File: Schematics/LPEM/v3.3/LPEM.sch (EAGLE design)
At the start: 40 parts, among them IC1 7805, IC2 PCA9600SO8, IC3 7803, IC4 7810, Q1 12MHz, U1 STM32F303K8T6, U2 MAX3421E

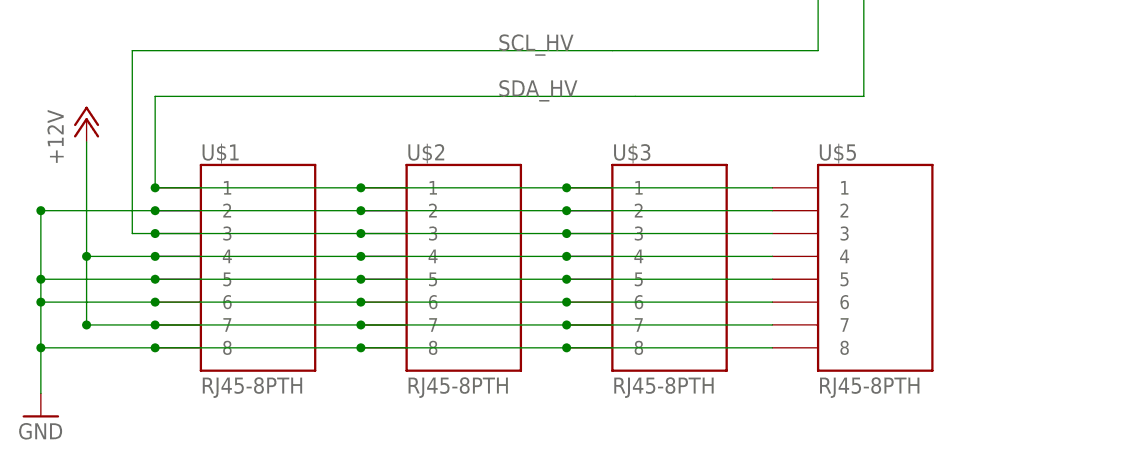
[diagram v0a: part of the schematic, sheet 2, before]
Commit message: Add LPEM v3.3, which will probably never be produced, and a few cleanups to other files.
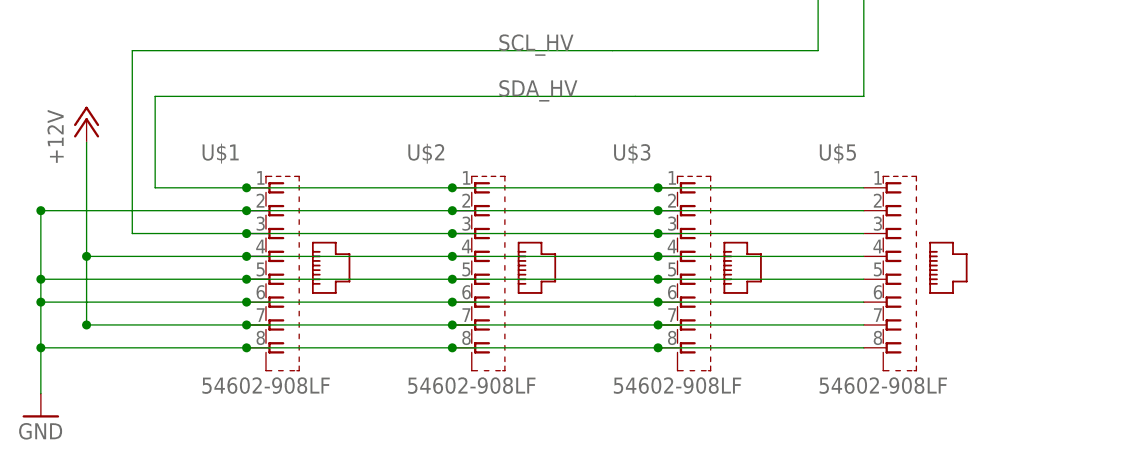
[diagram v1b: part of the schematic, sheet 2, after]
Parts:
- U$1, U$2, U$3, U$5: value RJ45-8PTH -> 54602-908LF; device SparkFun:RJ45-8PTH -> 54602-908LF:54602-908LF
